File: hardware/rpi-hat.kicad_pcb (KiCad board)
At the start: 2 copper layers, 65 x 56 mm, 49 parts, among them J1 Conn_02x20_Odd_Even__Rpi, J10 Conn_MQ_Gas, J11 Conn_MQ_Gas, J12 Conn_MQ_Gas, J13 Conn_MQ_Gas, J14 Conn_MQ_Gas, J15 Conn_MQ_Gas, J3 Conn_01x01_Female, J4 SM04B-SRSS-TB(LF)(SN), J5 SM04B-SRSS-TB(LF)(SN), J6 SM04B-SRSS-TB(LF)(SN), J7 Conn_01x02_Female, J8 10103594-0001LF, J9 Conn_01x02_Male, U1 CAT24C32WI-GT3, U2 ISO1H811G, U3 PCF8574T, U4 SN74LVC1G3157, U5 NCP699, U6 MCP3008T-I_SL, U7 SN74LV4T125PWR

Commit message: Update Schematic/Layout
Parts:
- removed the D1 at (207.1, 132.3)
- removed the J7 at (202.2, 135.7)
- removed the U2 at (231.9, 121.0)
- added D2: LED, Diode_SMD:D_0805_2012Metric, F.Cu at (292.6, 114.3)
- added D4: LED, Diode_SMD:D_0805_2012Metric, F.Cu at (219.5, 140.7)
- added D5: LED, Diode_SMD:D_0805_2012Metric, F.Cu at (225.6, 140.7)
- added D6: LED, Diode_SMD:D_0805_2012Metric, F.Cu at (233.3, 140.7)
- added D7: LED, Diode_SMD:D_0805_2012Metric, F.Cu at (240.3, 140.7)
- added D8: LED, Diode_SMD:D_0805_2012Metric, F.Cu at (247.9, 140.7)
- added D9: LED, Diode_SMD:D_0805_2012Metric, F.Cu at (254.0, 140.7)
- added J16: Conn_01x02_Male, zephyrus-iaq:PinHeader_1x02_P2.54mm_Vertical, F.Cu at (232.2, 112.3)
- added J9: SM03B-SRSS-TB(LF)(SN), zephyrus-iaq:JST_SM03B-SRSS-TB(LF)(SN), F.Cu at (219.2, 144.8)
- added R10: 330, Resistor_SMD:R_0805_2012Metric, F.Cu at (225.6, 135.6)
- added R11: 330, Resistor_SMD:R_0805_2012Metric, F.Cu at (233.2, 135.6)
- added R12: 330, Resistor_SMD:R_0805_2012Metric, F.Cu at (240.3, 135.6)
- added R13: 330, Resistor_SMD:R_0805_2012Metric, F.Cu at (247.9, 135.6)
- added R14: 330, Resistor_SMD:R_0805_2012Metric, F.Cu at (254.0, 135.6)
- added R15: 10k, Resistor_SMD:R_0805_2012Metric, F.Cu at (229.6, 176.8)
- added R16: 10k, Resistor_SMD:R_0805_2012Metric, F.Cu at (240.8, 176.3)
- added R17: 10k, Resistor_SMD:R_0805_2012Metric, F.Cu at (240.8, 165.6)
- added R18: 10k, Resistor_SMD:R_0805_2012Metric, F.Cu at (229.6, 165.1)
- added R19: 10K, Resistor_SMD:R_0805_2012Metric, F.Cu at (229.6, 173.2)
- added R20: 10K, Resistor_SMD:R_0805_2012Metric, F.Cu at (223.5, 113.3)
- added R21: 10K, Resistor_SMD:R_0805_2012Metric, F.Cu at (225.6, 113.4)
- added R22: 10K, Resistor_SMD:R_0805_2012Metric, F.Cu at (217.9, 129.5)
- added R6: 330, Resistor_SMD:R_0805_2012Metric, F.Cu at (296.7, 114.3)
- added R9: 330, Resistor_SMD:R_0805_2012Metric, F.Cu at (219.4, 135.6)
- added U1: DRV8837C, zephyrus-iaq:SON50P200X200X80-9N, F.Cu at (252.5, 113.8)
- added U8: SN74lV4051A, zephyrus-iaq:SOP65P640X120-16N, F.Cu at (223.0, 127.5)
- added U9: ADS1115IDGSR, zephyrus-iaq:SOP50P490X110-10N, F.Cu at (230.1, 115.8)
- C11: value 10uF -> 100nF
- C6: value 47uF -> 100nF
- C7: value 1uF -> 100nF
- C8: value 1uF -> 10uF
- D3: value 1N4728A_3.3V_100uA -> LED; footprint Diode_THT:D_DO-41_SOD81_P7.62mm_Horizontal -> Diode_SMD:D_0805_2012Metric
- J10, J11, J12, J13, J14: value Conn_MQ_Gas -> SM03B-SRSS-TB(LF)(SN); footprint Connector_PinSocket_2.00mm:PinSocket_1x03_P2.00mm_Horizontal -> zephyrus-iaq:JST_SM03B-SRSS-TB(LF)(SN)
- J15: value Conn_MQ_Gas -> Conn_01x01_Male; footprint Connector_PinSocket_2.00mm:PinSocket_1x03_P2.00mm_Horizontal -> zephyrus-iaq:PinHeader_1x01_P2.54mm_Vertical
- J2: value (none) -> USART 3.3V/5V; footprint S6B-ZR-SM4A-TF_LF__SN_:JST_S6B-ZR-SM4A-TF(LF)(SN) -> zephyrus-iaq:JST_SM04B-SRSS-TB(LF)(SN)
- J3: renamed from J4; value SM04B-SRSS-TB(LF)(SN) -> I2C 3.3V
- J4: renamed from J5; value SM04B-SRSS-TB(LF)(SN) -> I2C 3.3V
- J5: renamed from J6; value SM04B-SRSS-TB(LF)(SN) -> I2C 5V
- J6: renamed from J3; value Conn_01x01_Female -> PPS
- J8: renamed from J9; value Conn_01x02_Male -> Jumper
- R7: value 270 -> 330; footprint Resistor_SMD:R_0805_2012Metric_Pad1.15x1.40mm_HandSolder -> Resistor_SMD:R_0805_2012Metric
- U3: value PCF8574T -> AD8534; footprint zephyrus-iaq:SOIC127P1032X265-16N -> zephyrus-iaq:SOP65P640X120-14N
- U4: value SN74LVC1G3157 -> BSS138; footprint Package_TO_SOT_SMD:SOT-23-6 -> zephyrus-iaq:BSS138
- U5: value NCP699 -> BSS138; footprint Package_TO_SOT_SMD:SOT-23-5 -> zephyrus-iaq:BSS138
- U6: value MCP3008T-I_SL -> AD8532ARMZ-REEL; footprint MCP3008T-I_SL:SOIC127P600X175-16N -> zephyrus-iaq:SOIC127P600X175-8N
- U7: value SN74LV4T125PWR -> DAC43608; footprint SN74LV4T125PWR:SOP65P640X120-14N -> zephyrus-iaq:QFN50P300X300X80-17N
- moved MK1 81.9 mm to (203.6, 97.7)
- moved MK3 81.8 mm to (261.5, 97.5)
- moved R3 57.6 mm to (240.8, 172.7), turned to 0 degrees
- moved R4 50.8 mm to (229.6, 161.5), turned to 0 degrees
- moved MK4 48.3 mm to (261.5, 146.5)
- moved R7 45.7 mm to (296.2, 110.2)
- moved D3 43.2 mm to (292.6, 110.2), turned to 0 degrees
- moved MK2 34.3 mm to (203.6, 146.5)
- moved U4 32.9 mm to (222.0, 104.6)
- moved C4 31.9 mm to (254.5, 111.3), turned to 0 degrees
- moved C3 29.8 mm to (250.4, 111.3), turned to 180 degrees
- moved U5 29.2 mm to (227.1, 104.6)
- moved J15 29.0 mm to (221.0, 113.3), turned to 0 degrees
- moved J14 28.6 mm to (254.5, 144.8), turned to 0 degrees
- moved J10 27.4 mm to (226.1, 144.8), turned to 0 degrees
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- renumbered D2 to D1, J8 to J7, R6 to R8, U1 to U2
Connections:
- net GPS_PPS renamed /GPIO18(GEN1)(PWM0)
- net ID_SD_EEPROM renamed /ID_SD_EEPROM
- C3 pad 1: +3V3 -> +5V
- C8 pad 1: /Analog_Sensors/1V4 -> +5V
- D3 pad 1: /GPIO9(SPI0_MISO) -> Net-(D3-Pad1)
- D3 pad 2: GND -> /FAN_OUT2
- F1 pad 1: +5V -> Net-(F1-Pad1)
- F1 pad 2: Net-(F1-Pad2) -> +5V
- J1 pad 10: RXD0 -> /GPIO15(RXD0)
- J1 pad 16: /GPIO23(GEN4) -> /DAC_CLR_pu
- J1 pad 22: /GPIO25(GEN6) -> /FAN_nSLEEP
- J1 pad 3: SDA -> /GPIO2(SDA1)
- J1 pad 32: /GPIO12(PWM0) -> /FAN_PWM0
- J1 pad 33: /GPIO13(PWM1) -> /FAN_PWM1
- J1 pad 5: SCL -> /GPIO3(SCL1)
- J1 pad 8: TXD0 -> /GPIO14(TXD0)
- J10 pad 1: /Analog_Sensors/Vswitch0 -> /Analog_Sensors/BUF_OUT_1
- J10 pad 3: /ADC0 -> /ADC3
- J11 pad 1: /Analog_Sensors/Vswitch1 -> /Analog_Sensors/BUF_OUT_2
- J12 pad 1: /Analog_Sensors/Vswitch2 -> /Analog_Sensors/BUF_OUT_3
- J12 pad 3: /ADC2 -> /ADC4
- J13 pad 1: /Analog_Sensors/Vswitch3 -> /Analog_Sensors/BUF_OUT_4
- J13 pad 3: /ADC3 -> /ADC2
- J14 pad 1: /Analog_Sensors/Vswitch4 -> /Analog_Sensors/BUF_OUT_5
- J14 pad 3: /ADC4 -> /ADC5
- J15 pad 1: /Analog_Sensors/5V_1V4_0V -> /ADC_Subsystem/ADC_ALERT
- J2 pad 1: +5V -> /GPIO15(RXD0)
- J2 pad 2: GND -> /GPIO14(TXD0)
- J2 pad 3: RXD0 -> GND
- J2 pad 4: TXD0 -> +5V
- J3 pad 1: SCL -> GND
- J3 pad 2: SDA -> +3V3
- J3 pad 3: +3V3 -> /GPIO2(SDA1)
- J3 pad 4: GND -> /GPIO3(SCL1)
- J4 pad 1: SCL -> GND
- J4 pad 2: SDA -> +3V3
- J4 pad 3: +3V3 -> /GPIO3(SCL1)
- J4 pad 4: GND -> /GPIO2(SDA1)
- J5 pad 1: SCL -> GND
- J5 pad 2: SDA -> +5V
- J5 pad 3: +3V3 -> /SDA_5
- J5 pad 4: GND -> /SCL_5
- J7 pad 1: Net-(F1-Pad2) -> Net-(F1-Pad1)
- R3 pad 2: SDA -> /GPIO2(SDA1)
- R4 pad 2: SCL -> /GPIO3(SCL1)
- R7 pad 1: Net-(R7-Pad1) -> Net-(D3-Pad1)
- R7 pad 2: /GPIO9(SPI0_MISO) -> GND
- U3 pad 1: GND -> /Analog_Sensors/BUF_OUT_1
- U3 pad 10: /Analog_Sensors/D5 -> /Analog_Sensors/DAC_OUT_D
- U3 pad 11: /Analog_Sensors/D6 -> GND
- U3 pad 12: /Analog_Sensors/D7 -> /Analog_Sensors/DAC_OUT_C
- U3 pad 13: GND -> /Analog_Sensors/BUF_OUT_2
- U3 pad 14: SCL -> /Analog_Sensors/BUF_OUT_2
- U3 pad 2: GND -> /Analog_Sensors/BUF_OUT_1
- U3 pad 3: GND -> /Analog_Sensors/DAC_OUT_B
- U3 pad 4: /Analog_Sensors/D0 -> +5V
- U3 pad 5: /Analog_Sensors/D1 -> /Analog_Sensors/DAC_OUT_A
- U3 pad 6: /Analog_Sensors/D2 -> /Analog_Sensors/BUF_OUT_0
- U3 pad 7: /Analog_Sensors/D3 -> /Analog_Sensors/BUF_OUT_0
- U3 pad 8: GND -> /Analog_Sensors/BUF_OUT_3
- U3 pad 9: /Analog_Sensors/D4 -> /Analog_Sensors/BUF_OUT_3
- U6 pad 1: /ADC0 -> /Analog_Sensors/BUF_OUT_4
- U6 pad 2: /ADC1 -> /Analog_Sensors/BUF_OUT_4
- U6 pad 3: /ADC2 -> /Analog_Sensors/DAC_OUT_F
- U6 pad 4: /ADC3 -> GND
- U6 pad 5: /ADC4 -> /Analog_Sensors/DAC_OUT_E
- U6 pad 6: /ADC5 -> /Analog_Sensors/BUF_OUT_5
- U6 pad 7: /ADC6 -> /Analog_Sensors/BUF_OUT_5
- U6 pad 8: /ADC7 -> +5V
- U7 pad 1: GND -> /Analog_Sensors/DAC_OUT_A
- U7 pad 10: GND -> /Analog_Sensors/DAC_OUT_F
- U7 pad 13: GND -> +5V
- U7 pad 14: +5V -> GND
- U7 pad 2: /GPIO10(SPI0_MOSI) -> /Analog_Sensors/DAC_OUT_B
- U7 pad 3: /ADC_Subsystem/MOSI_5 -> /Analog_Sensors/DAC_OUT_C
- U7 pad 4: GND -> /Analog_Sensors/DAC_OUT_D
- U7 pad 5: /GPIO11(SPI0_SCK) -> /SDA_5
- U7 pad 6: /ADC_Subsystem/SCK_5 -> /SCL_5
- U7 pad 8: /ADC_Subsystem/~CE~_5 -> GND
- U7 pad 9: /GPIO8(SPI0_CE_N) -> /Analog_Sensors/DAC_OUT_E
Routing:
- net GND: track 129.6 -> 284.4 mm, vias 25 -> 34
- net SDA: track 107.2 -> 0.00 mm, vias 2 -> 0
- net /GPIO2(SDA1): track 0.00 -> 107.2 mm, vias 0 -> 2
- net /GPIO3(SCL1): track 0.00 -> 90.6 mm, vias 0 -> 3
- net SCL: track 89.2 -> 0.00 mm, vias 2 -> 0
- net /Analog_Sensors/BUF_OUT_0: track 0.00 -> 85.3 mm, vias 0 -> 1
- net /Analog_Sensors/DAC_OUT_B: track 0.00 -> 49.0 mm, vias 0 -> 1
- net /Vfan: track 47.0 -> 0.00 mm
- net /Analog_Sensors/BUF_OUT_5: track 0.00 -> 43.1 mm, vias 0 -> 1
- net /Analog_Sensors/Vswitch0: track 37.7 -> 0.00 mm, vias 1 -> 0
- net /Analog_Sensors/Vswitch5: track 31.7 -> 0.00 mm, vias 2 -> 0
- net /ADC5: track 32.4 -> 1.58 mm
- net /Analog_Sensors/Vswitch4: track 30.2 -> 0.00 mm, vias 1 -> 0
- net +5V: track 55.6 -> 85.6 mm, vias 7 -> 3
- net /Analog_Sensors/Vswitch6: track 28.6 -> 0.00 mm, vias 2 -> 0
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
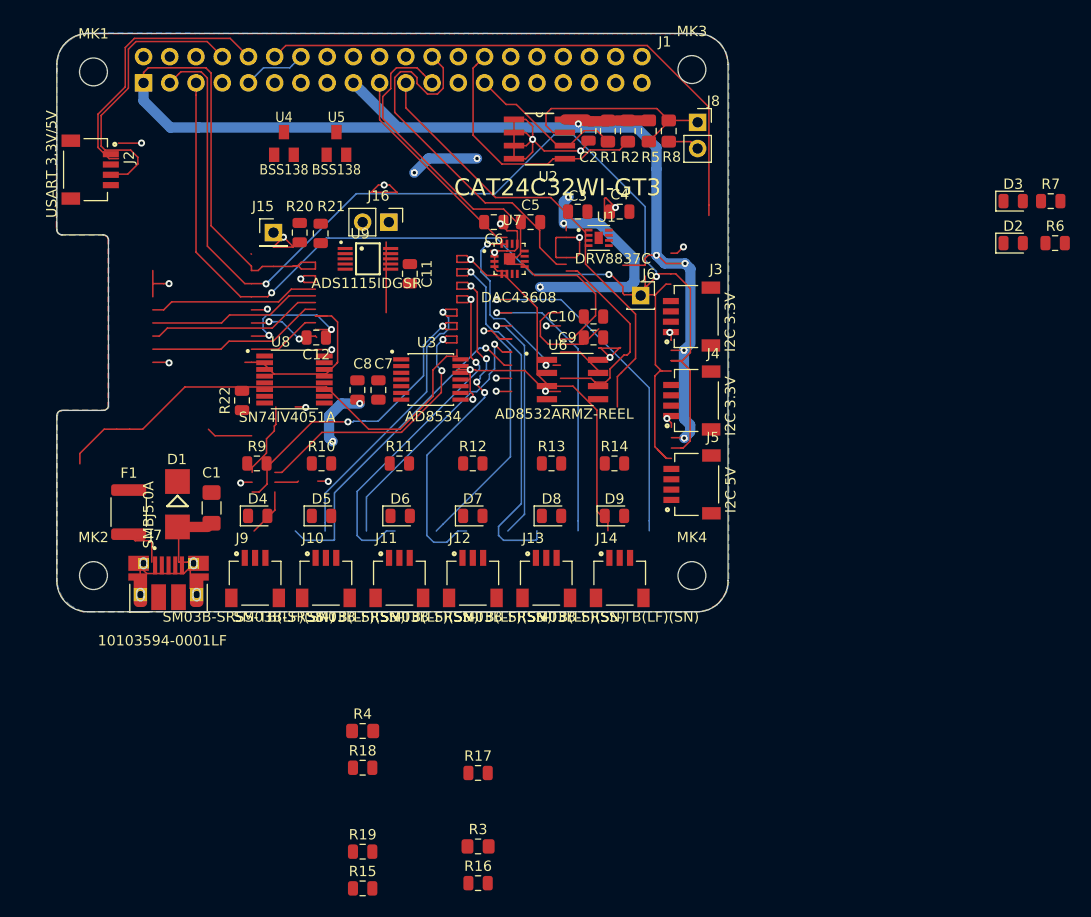
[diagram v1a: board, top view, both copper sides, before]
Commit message: Update KiCad Layout
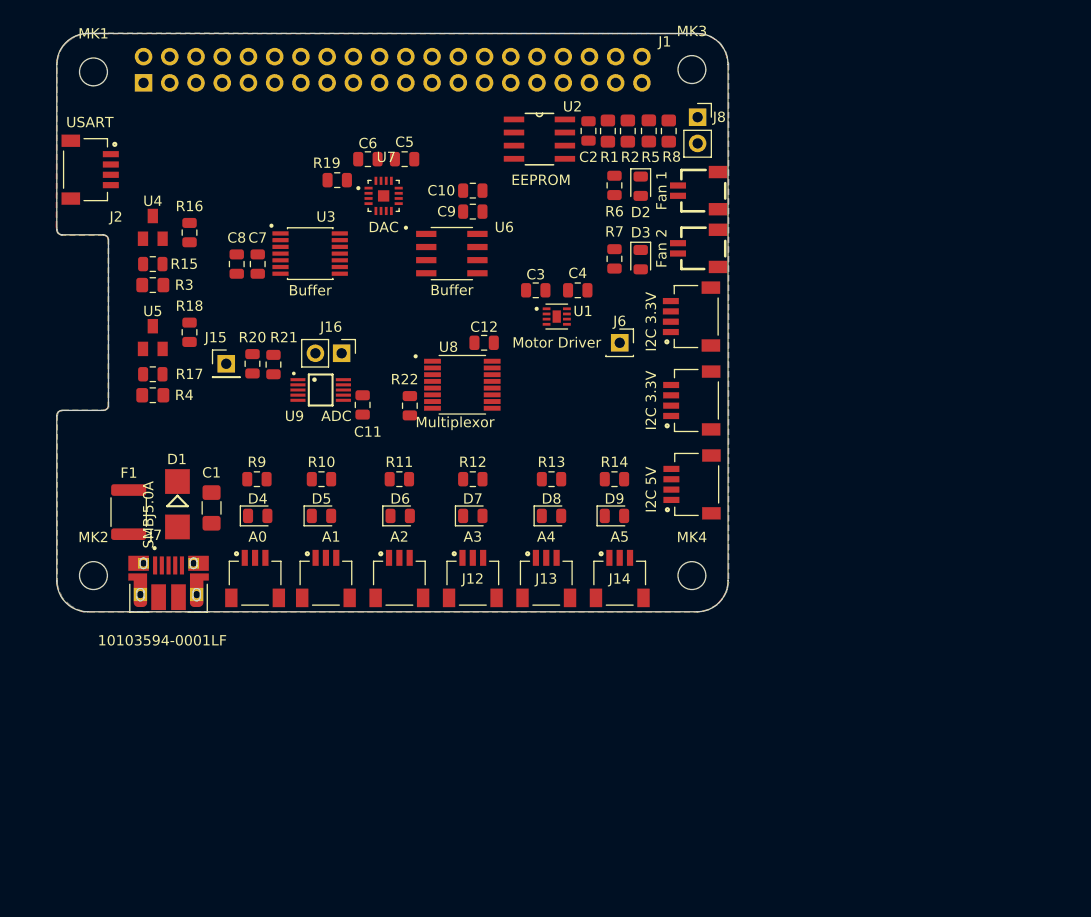
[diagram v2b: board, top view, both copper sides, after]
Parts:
- added J17: Fan 1, zephyrus-iaq:SM02B-SRSS-TB(LF)(SN), F.Cu at (262.1, 109.2)
- added J18: Fan 2, zephyrus-iaq:SM02B-SRSS-TB(LF)(SN), F.Cu at (262.1, 114.8)
- J10: value SM03B-SRSS-TB(LF)(SN) -> A1
- J11: value SM03B-SRSS-TB(LF)(SN) -> A2
- J12: value SM03B-SRSS-TB(LF)(SN) -> A3
- J13: value SM03B-SRSS-TB(LF)(SN) -> A4
- J14: value SM03B-SRSS-TB(LF)(SN) -> A5
- J2: value USART 3.3V/5V -> USART
- J9: value SM03B-SRSS-TB(LF)(SN) -> A0
- U1: value DRV8837C -> Motor Driver
- U2: value CAT24C32WI-GT3 -> EEPROM
- U3: value AD8534 -> Buffer
- U5: value BSS138 -> BSS18
- U6: value AD8532ARMZ-REEL -> Buffer
- U7: value DAC43608 -> DAC
- U8: value SN74lV4051A -> Multiplexor
- U9: value ADS1115IDGSR -> ADC
- moved R16 68.9 mm to (212.9, 113.3), turned to 90 degrees
- moved R19 65.1 mm to (227.2, 108.2)
- moved R15 63.8 mm to (209.3, 116.3)
- moved R3 62.8 mm to (209.3, 118.4)
- moved R17 49.8 mm to (209.3, 127.0)
- moved R18 45.4 mm to (212.9, 122.9), turned to 90 degrees
- moved R6 43.0 mm to (254.0, 108.7), turned to 270 degrees
- moved R7 42.6 mm to (254.0, 115.8), turned to 270 degrees
- moved R4 38.3 mm to (209.3, 129.0)
- moved D3 36.5 mm to (256.5, 115.9), turned to 270 degrees
- moved D2 36.5 mm to (256.5, 108.8), turned to 270 degrees
- moved U5 25.9 mm to (209.3, 123.4)
- moved C10 16.9 mm to (240.3, 109.2)
- moved C7 16.9 mm to (219.5, 116.3)
- moved C8 16.9 mm to (217.4, 116.3)
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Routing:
- net GND: track 284.4 -> 0.00 mm, vias 34 -> 0
- net +3V3: track 150.1 -> 0.00 mm, vias 5 -> 0
- net /GPIO2(SDA1): track 107.2 -> 0.00 mm, vias 2 -> 0
- net /GPIO3(SCL1): track 90.6 -> 0.00 mm, vias 3 -> 0
- net +5V: track 85.6 -> 0.00 mm, vias 3 -> 0
- net /Analog_Sensors/BUF_OUT_0: track 85.3 -> 0.00 mm, vias 1 -> 0
- net /GPIO18(GEN1)(PWM0): track 55.5 -> 0.00 mm
- net /Analog_Sensors/DAC_OUT_B: track 49.0 -> 0.00 mm, vias 1 -> 0
- net /GPIO9(SPI0_MISO): track 44.5 -> 0.00 mm
- net /Analog_Sensors/BUF_OUT_5: track 43.1 -> 0.00 mm, vias 1 -> 0
- net /Analog_Sensors/Vswitch1: track 37.1 -> 0.00 mm, vias 1 -> 0
- net /GPIO8(SPI0_CE_N): track 36.9 -> 0.00 mm
- net /Analog_Sensors/Vswitch2: track 36.2 -> 0.00 mm, vias 4 -> 0
- net /Analog_Sensors/Vswitch3: track 36.0 -> 0.00 mm, vias 2 -> 0
- net /ADC0: track 33.6 -> 0.00 mm, vias 1 -> 0
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
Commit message: KiCad Layout Update
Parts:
- J10: value A1 -> SM03B-SRSS-TB(LF)(SN)
- J11: value A2 -> SM03B-SRSS-TB(LF)(SN)
- J12: value A3 -> SM03B-SRSS-TB(LF)(SN)
- J13: value A4 -> SM03B-SRSS-TB(LF)(SN)
- J14: value A5 -> SM03B-SRSS-TB(LF)(SN)
- J17: value Fan 1 -> SM02B-SRSS-TB(LF)(SN)
- J18: value Fan 2 -> SM02B-SRSS-TB(LF)(SN)
- J2: value USART -> USART 3.3V/5V
- J9: value A0 -> SM03B-SRSS-TB(LF)(SN)
- U1: value Motor Driver -> DRV8837C
- U2: value EEPROM -> CAT24C32WI-GT3
- U3: value Buffer -> AD8534
- U5: value BSS18 -> BSS138
- U6: value Buffer -> AD8532ARMZ-REEL
- U7: value DAC -> DAC43608
- U8: value Multiplexor -> SN74lV4051A
- U9: value ADC -> ADS1115IDGSR
- moved R22 2.54 mm to (236.7, 130.0)
- moved C12 2.54 mm to (243.9, 124.0)
- moved U8 2.54 mm to (241.8, 128.0)
- moved D8 0.51 mm to (247.4, 140.7)
- moved D9 0.51 mm to (254.5, 140.7)
- moved R13 0.51 mm to (247.4, 137.2)
- moved R14 0.51 mm to (254.5, 137.2)
- moved J3 0.51 mm to (260.0, 121.4)
- moved J4 0.51 mm to (260.0, 129.5)
- moved J5 0.51 mm to (260.0, 137.7)
- moved J7 0.41 mm to (210.5, 148.1)
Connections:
- J10 pad 3: /ADC3 -> /ADC1
- J11 pad 3: /ADC1 -> /ADC2
- J12 pad 3: /ADC4 -> /ADC3
- J13 pad 3: /ADC2 -> /ADC4
- U3 pad 10: /Analog_Sensors/DAC_OUT_D -> /Analog_Sensors/DAC_OUT_C
- U3 pad 12: /Analog_Sensors/DAC_OUT_C -> /Analog_Sensors/DAC_OUT_D
- U3 pad 13: /Analog_Sensors/BUF_OUT_2 -> /Analog_Sensors/BUF_OUT_3
- U3 pad 14: /Analog_Sensors/BUF_OUT_2 -> /Analog_Sensors/BUF_OUT_3
- U3 pad 8: /Analog_Sensors/BUF_OUT_3 -> /Analog_Sensors/BUF_OUT_2
- U3 pad 9: /Analog_Sensors/BUF_OUT_3 -> /Analog_Sensors/BUF_OUT_2
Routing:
- net +3V3: track 0.00 -> 118.8 mm, vias 0 -> 5
- net /SDA_5: track 0.00 -> 103.5 mm, vias 0 -> 6
- net GND: track 0.00 -> 99.9 mm, vias 0 -> 35
- net /SCL_5: track 0.00 -> 75.2 mm, vias 0 -> 4
- net +5V: track 0.00 -> 73.3 mm, vias 0 -> 14
- net /GPIO17(GEN0): track 0.00 -> 65.2 mm, vias 0 -> 1
- net /GPIO27(GEN2): track 0.00 -> 63.6 mm, vias 0 -> 1
- net /GPIO22(GEN3): track 0.00 -> 60.9 mm, vias 0 -> 1
- net /FAN_nSLEEP: track 0.00 -> 58.9 mm, vias 0 -> 1
- net /ADC0: track 0.00 -> 55.5 mm
- net /FAN_PWM1: track 0.00 -> 53.0 mm
- net /GPIO18(GEN1)(PWM0): track 0.00 -> 52.7 mm, vias 0 -> 1
- net /FAN_PWM0: track 0.00 -> 49.8 mm
- net /ADC1: track 0.00 -> 49.8 mm, vias 0 -> 2
- net /Analog_Sensors/BUF_OUT_4: track 0.00 -> 49.2 mm
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
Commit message: PCB Complete.  Pending Review.
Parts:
- J10: value SM03B-SRSS-TB(LF)(SN) -> A1
- J11: value SM03B-SRSS-TB(LF)(SN) -> A2
- J12: value SM03B-SRSS-TB(LF)(SN) -> A3
- J13: value SM03B-SRSS-TB(LF)(SN) -> A4
- J14: value SM03B-SRSS-TB(LF)(SN) -> A5
- J17: value SM02B-SRSS-TB(LF)(SN) -> Fan 1
- J18: value SM02B-SRSS-TB(LF)(SN) -> Fan 2
- J2: value USART 3.3V/5V -> USART
- J9: value SM03B-SRSS-TB(LF)(SN) -> A0
- U1: value DRV8837C -> Fan Driver
- U2: value CAT24C32WI-GT3 -> EEPROM
- U3: value AD8534 -> Buffer
- U6: value AD8532ARMZ-REEL -> Buffer
- U7: value DAC43608 -> DAC
- U8: value SN74lV4051A -> Multiplexor
- U9: value ADS1115IDGSR -> ADC
- moved U2 2.39 mm to (244.3, 104.2)
- moved J6 2.27 mm to (255.5, 121.9)
- moved R8 1.22 mm to (259.1, 104.7)
- moved J8 0.77 mm to (262.6, 102.6)
- moved J15 0.72 mm to (215.9, 126.5)
- moved C2 0.53 mm to (251.0, 103.4)
- moved R1 0.38 mm to (253.0, 103.5)
- moved R2 0.28 mm to (255.0, 103.5)
- moved R5 0.28 mm to (257.0, 103.4)
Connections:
- J7 pad S3: GND -> Net-(J7-PadS3)
- J7 pad S4: GND -> Net-(J7-PadS4)
- J7 pad S5: GND -> Net-(J7-PadS5)
- J7 pad S6: GND -> Net-(J7-PadS6)
- U7 pad 17: (no net) -> GND
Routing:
- net /GPIO3(SCL1): track 46.8 -> 126.6 mm
- net /GPIO2(SDA1): track 32.5 -> 104.4 mm, vias 0 -> 1
- net +5V: track 73.3 -> 117.2 mm, vias 14 -> 19
- net +3V3: track 118.8 -> 157.3 mm, vias 5 -> 6
- net GND: track 99.9 -> 133.1 mm, vias 35 -> 38
- net Net-(J8-Pad1): track 14.3 -> 18.8 mm
- net /FAN_PWM0: track 49.8 -> 54.3 mm
- net /FAN_nSLEEP: track 58.9 -> 61.5 mm
- net /GPIO18(GEN1)(PWM0): track 52.7 -> 51.1 mm
- net /ID_SD_EEPROM: track 16.8 -> 15.3 mm
- net /FAN_PWM1: track 53.0 -> 54.1 mm
- net /ADC0: track 55.5 -> 56.3 mm
- net /ID_SC_EEPROM: track 25.7 -> 24.9 mm
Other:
- board text added: "Addr Sel"
- board text added: "Alert"
- board text added: "PPS"
